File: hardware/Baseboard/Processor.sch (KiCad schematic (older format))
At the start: 29 parts, among them IC1 74HC00, IC10 W65C22, IC2 W65C02, IC3 74HC138, IC4 SYSTEM ROM, IC5 RAM, IC6 W65C22, IC7 W65C51, SW6 CLOCK, SW7 CLOCK INPUT

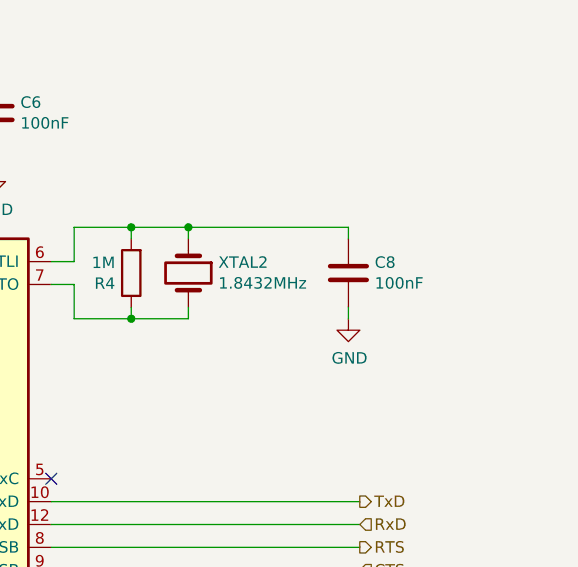
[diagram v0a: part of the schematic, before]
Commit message: Change C8 to 30 pF
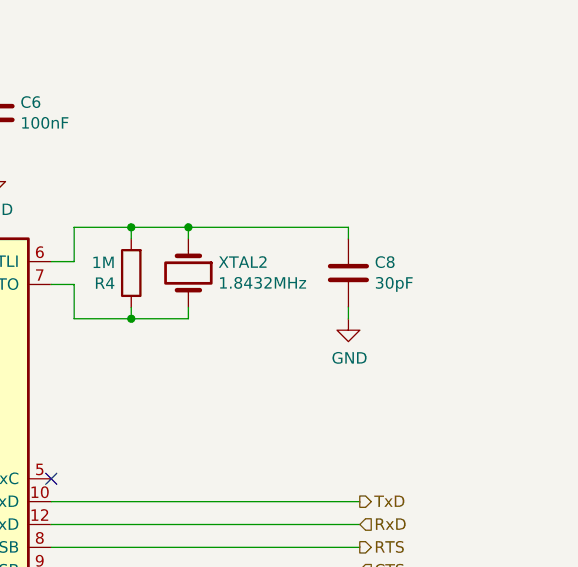
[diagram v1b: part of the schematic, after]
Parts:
- C8: value 100nF -> 30pF; Mfr. TDK -> Kemet; Mfr. No. FA18X8R1H104KRU06 -> C315C300JCG5TA; Mouser 810-FA18X8R1H104KRU6 -> 80-C315C300JCG5TA
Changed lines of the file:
@@
 AR Path="/5EB09E21/5F17EFA5" Ref="C8"  Part="1"
 F 0 "C8" H 13965 6196 50  0000 L CNN
-F 1 "100nF" H 13965 6105 50  0000 L CNN
+F 1 "30pF" H 13965 6105 50  0000 L CNN
 F 2 "Capacitor_THT:C_Rect_L4.0mm_W2.5mm_P2.50mm" H 13888 6000 50  0001 C CNN
 F 3 "https://www.mouser.de/datasheet/2/400/eadmlcc_halogenfree_fa150_en-890480.pdf" H 13850 6150 50  0001 C CNN
-F 4 "TDK" H 13850 6150 50  0001 C CNN "Mfr."
-F 5 "FA18X8R1H104KRU06" H 13850 6150 50  0001 C CNN "Mfr. No."
-F 6 "810-FA18X8R1H104KRU6" H 13850 6150 50  0001 C CNN "Mouser"
+F 4 "Kemet" H 13850 6150 50  0001 C CNN "Mfr."
+F 5 "C315C300JCG5TA" H 13850 6150 50  0001 C CNN "Mfr. No."
+F 6 "80-C315C300JCG5TA" H 13850 6150 50  0001 C CNN "Mouser"
 	1    13850 6150
 	1    0    0    -1
